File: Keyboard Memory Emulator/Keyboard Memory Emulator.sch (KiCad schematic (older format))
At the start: 14 parts, among them J1 Conn_01x05, J2 Conn_01x01_Male, J3 Conn_01x02, J5 Conn_01x02, J6 Conn_01x04, J7 Conn_01x05, J8 Conn_02x05_Odd_Even, U5 SN74HC244APWR, U6 IS62C256AL-45ULI-TR

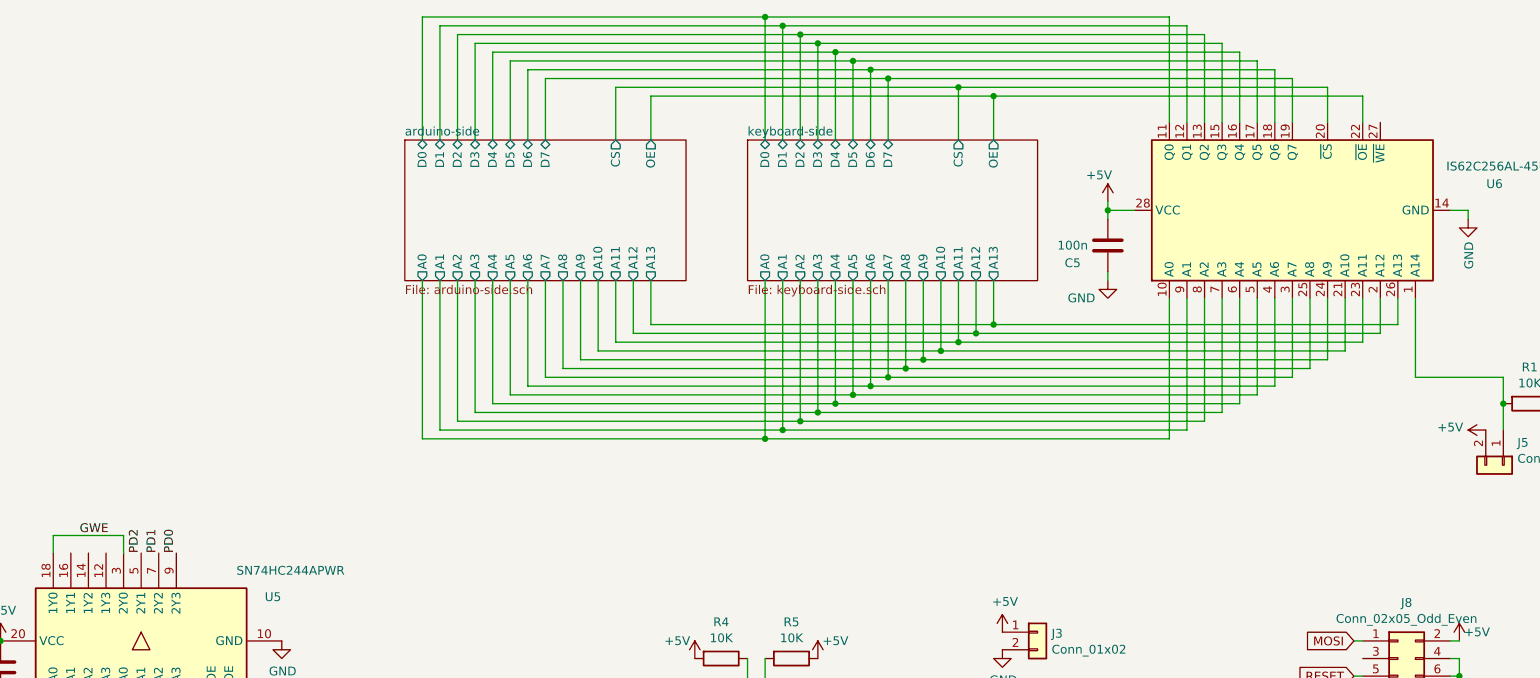
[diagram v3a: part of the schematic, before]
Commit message: Added a gitignore, hopefully it will work as I hope. I also fixed the traces that were not showing up due to improper nets.
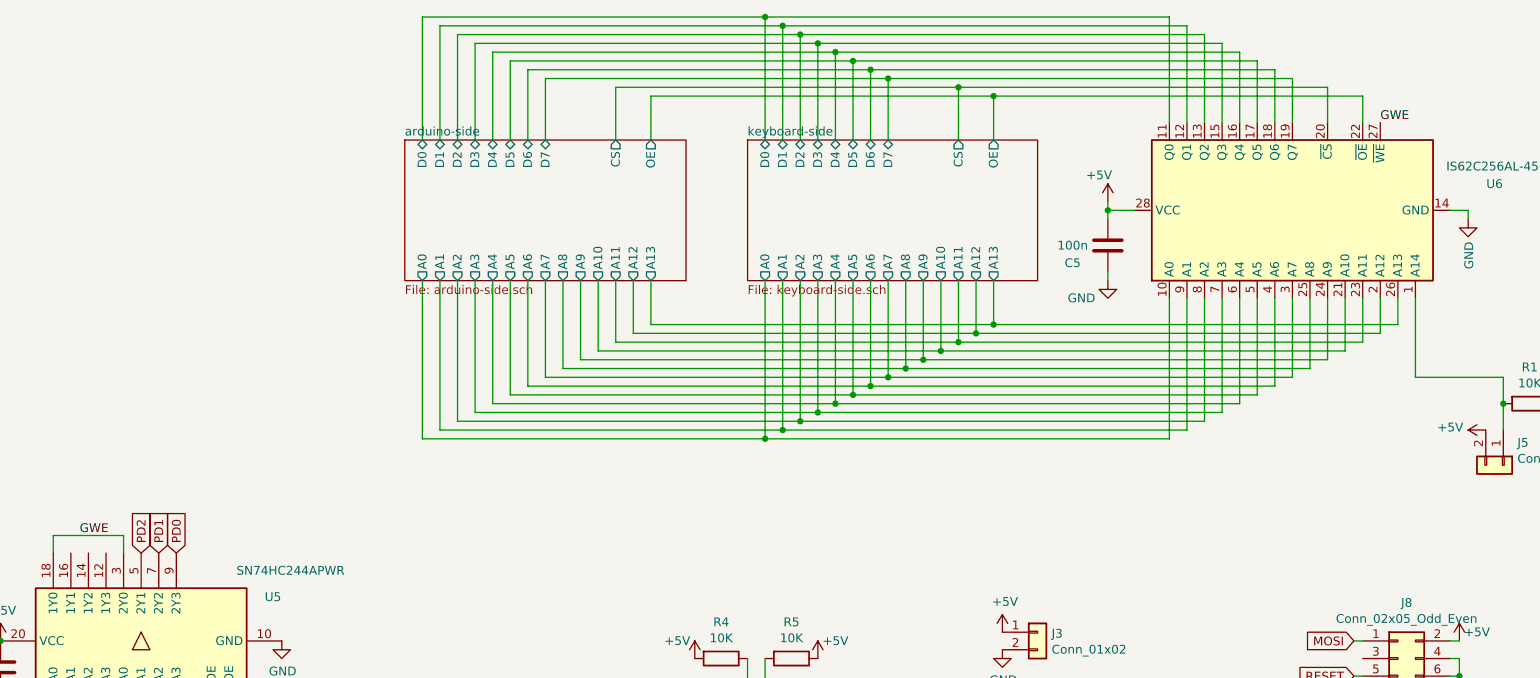
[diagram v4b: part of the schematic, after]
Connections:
- net GWE: now also U6.27 (~WE)
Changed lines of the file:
@@
 Sheet 1 3
 Title "Keyboard Memory Emulator"
-Date "2020-11-29"
-Rev "P-0"
+Date "2020-12-22"
+Rev "P-1"
 Comp "Mason Gulu, Lucas Christy"
 Comment1 ""
@@
 $EndComp
 Connection ~ 9700 3600
-Text Label 1950 4450 1    50   ~ 0
-PD2
-Text Label 2050 4450 1    50   ~ 0
-PD1
-Text Label 2150 4450 1    50   ~ 0
-PD0
 $Comp
 L power:+5V #PWR0129
@@
 	1    0    0    -1
 $EndComp
+Text Label 9000 2000 0    50   ~ 0
+GWE
+Text GLabel 2150 4450 1    50   Input ~ 0
+PD0
+Text GLabel 2050 4450 1    50   Input ~ 0
+PD1
+Text GLabel 1950 4450 1    50   Input ~ 0
+PD2
 $EndSCHEMATC
